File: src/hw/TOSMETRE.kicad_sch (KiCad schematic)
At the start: 61 parts, among them J1 Barrel_Jack_Switch, J2 Conn_01x02_Male, J3 Conn_01x08_Male, J4 Conn_Coaxial, J5 Conn_01x05_Male, J6 Conn_01x02_Male, J7 Conn_Coaxial, SW1 SW_DIP_x01, U1 TPS70950DBVT, U2 18F1320, U3 LT1818, U4 LTC2305, U5 LT1818

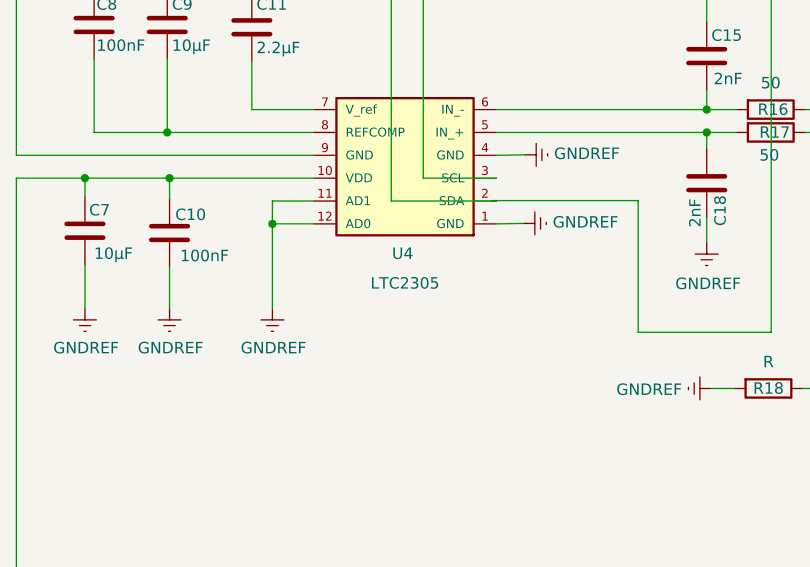
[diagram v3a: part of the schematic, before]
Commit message: #406
erreur danns la net liste
le U4 etait un 8plot alors qu'il en faut 12
rectif faite
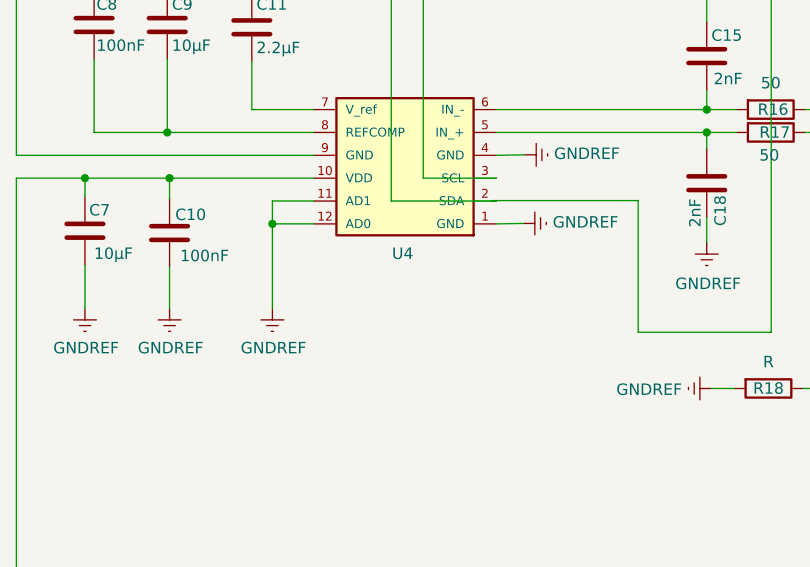
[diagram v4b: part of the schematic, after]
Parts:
- U4: value LTC2305 -> (none); footprint Package_SO:MSOP-8_3x3mm_P0.65mm -> (none)
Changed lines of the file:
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@@
     (in_bom yes) (on_board yes)
     (property "Reference" "U4" (id 0) (at 242.062 122.682 0))
-    (property "Value" "LTC2305" (id 1) (at 242.316 125.984 0))
-    (property "Footprint" "Package_SO:MSOP-8_3x3mm_P0.65mm" (id 2) (at 266.446 104.14 0)
+    (property "Value" "" (id 1) (at 242.316 125.984 0))
+    (property "Footprint" "" (id 2) (at 266.446 104.14 0)
       (effects (font (size 1.27 1.27)) hide)
     )
@@
     )
     (path "/00000000-0000-0000-0000-0000604b2f63"
-      (reference "U4") (unit 1) (value "LTC2305") (footprint "Package_SO:MSOP-8_3x3mm_P0.65mm")
+      (reference "U4") (unit 1) (value "LTC2305") (footprint "Package_SO:MSOP-12_3x4mm_P0.65mm")
     )
     (path "/00000000-0000-0000-0000-000060639a0d"

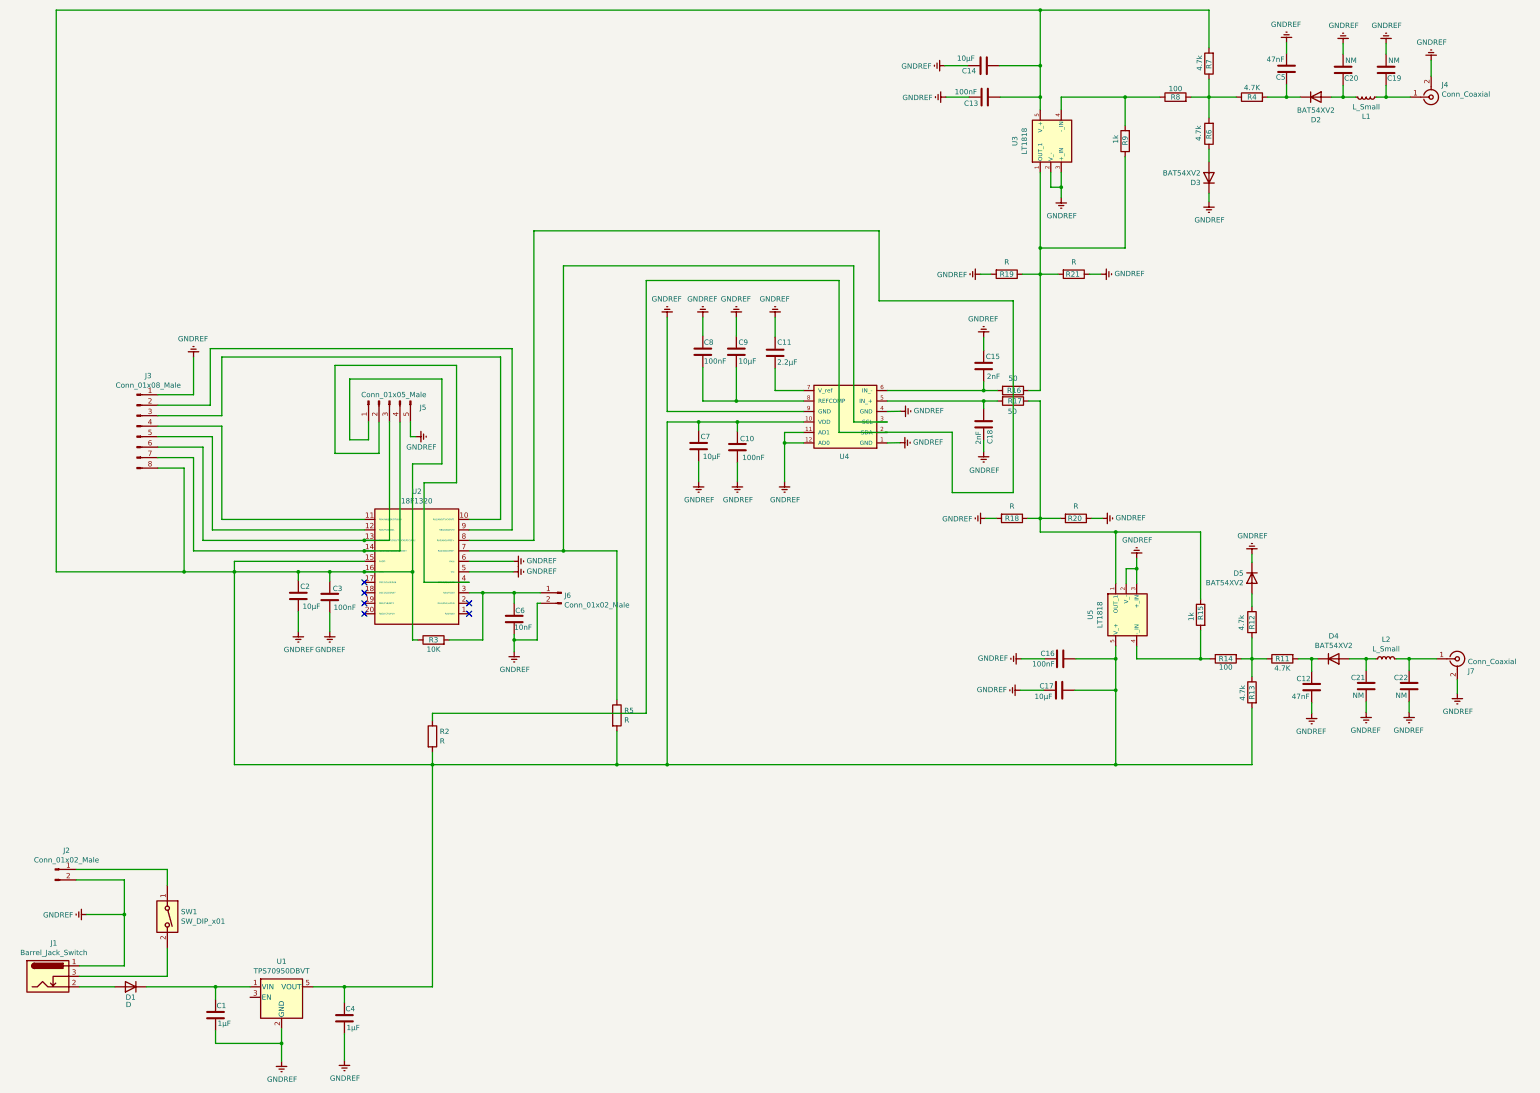
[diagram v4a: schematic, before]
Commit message: #406
PB termine
Nouvelle appleation suite a mauvaise manip (GRRRR) desole

Voir si on peux pas changer R1et R2 pour eviter qu'une piste passe dessous
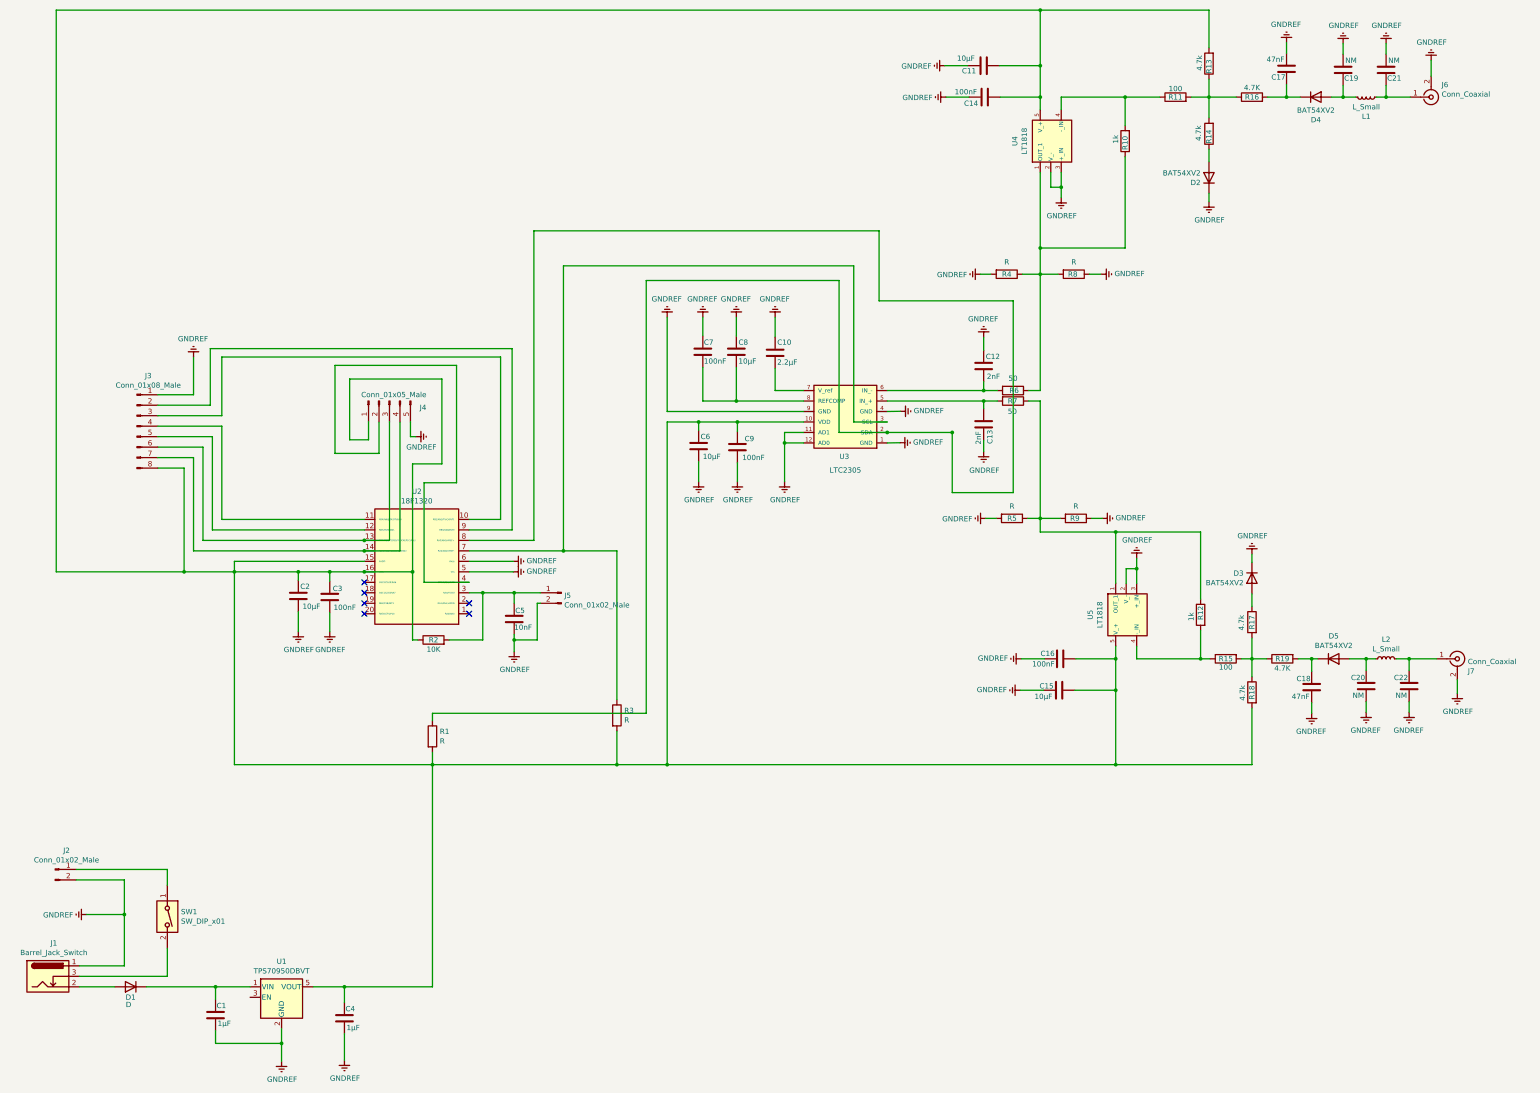
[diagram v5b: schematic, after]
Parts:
- U3: renamed from U4; value (none) -> LTC2305; footprint (none) -> Package_SO:MSOP-12_3x4mm_P0.65mm
- renumbered C11 to C10, C14 to C11, C15 to C12, C18 to C13, C13 to C14, C17 to C15, C5 to C17, C12 to C18, C20 to C19, C21 to C20, C19 to C21, C6 to C5, C7 to C6, C8 to C7, C9 to C8, C10 to C9, D3 to D2, D5 to D3, D2 to D4, D4 to D5, J5 to J4, J6 to J5, J4 to J6, R2 to R1, R9 to R10, R8 to R11, R15 to R12, R7 to R13, R6 to R14, R14 to R15, R4 to R16, R12 to R17, R13 to R18, R11 to R19, R3 to R2, R5 to R3, R19 to R4, R18 to R5, R16 to R6, R17 to R7, R21 to R8, R20 to R9, U3 to U4
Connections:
- net at U2.8 (RA3/AN3/VREF+): now also R1.1, U3.2 (SDA)

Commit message: #406
test
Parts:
- U4: renamed from U3; value LTC2305 -> (none); footprint Package_SO:MSOP-12_3x4mm_P0.65mm -> (none)
- renumbered C9 to C10, C10 to C11, C18 to C12, C14 to C13, C11 to C14, C12 to C15, C15 to C17, C13 to C18, C21 to C19, C19 to C20, C20 to C21, C17 to C5, C5 to C6, C6 to C7, C7 to C8, C8 to C9, D4 to D2, D2 to D3, D5 to D4, D3 to D5, J6 to J4, J4 to J5, J5 to J6, R19 to R11, R17 to R12, R18 to R13, R15 to R14, R12 to R15, R6 to R16, R7 to R17, R5 to R18, R4 to R19, R1 to R2, R9 to R20, R8 to R21, R2 to R3, R16 to R4, R3 to R5, R14 to R6, R13 to R7, R11 to R8, R10 to R9, U4 to U3
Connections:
- net at R2.1, U4.2 (SDA): no longer U2.8 (RA3/AN3/VREF+)

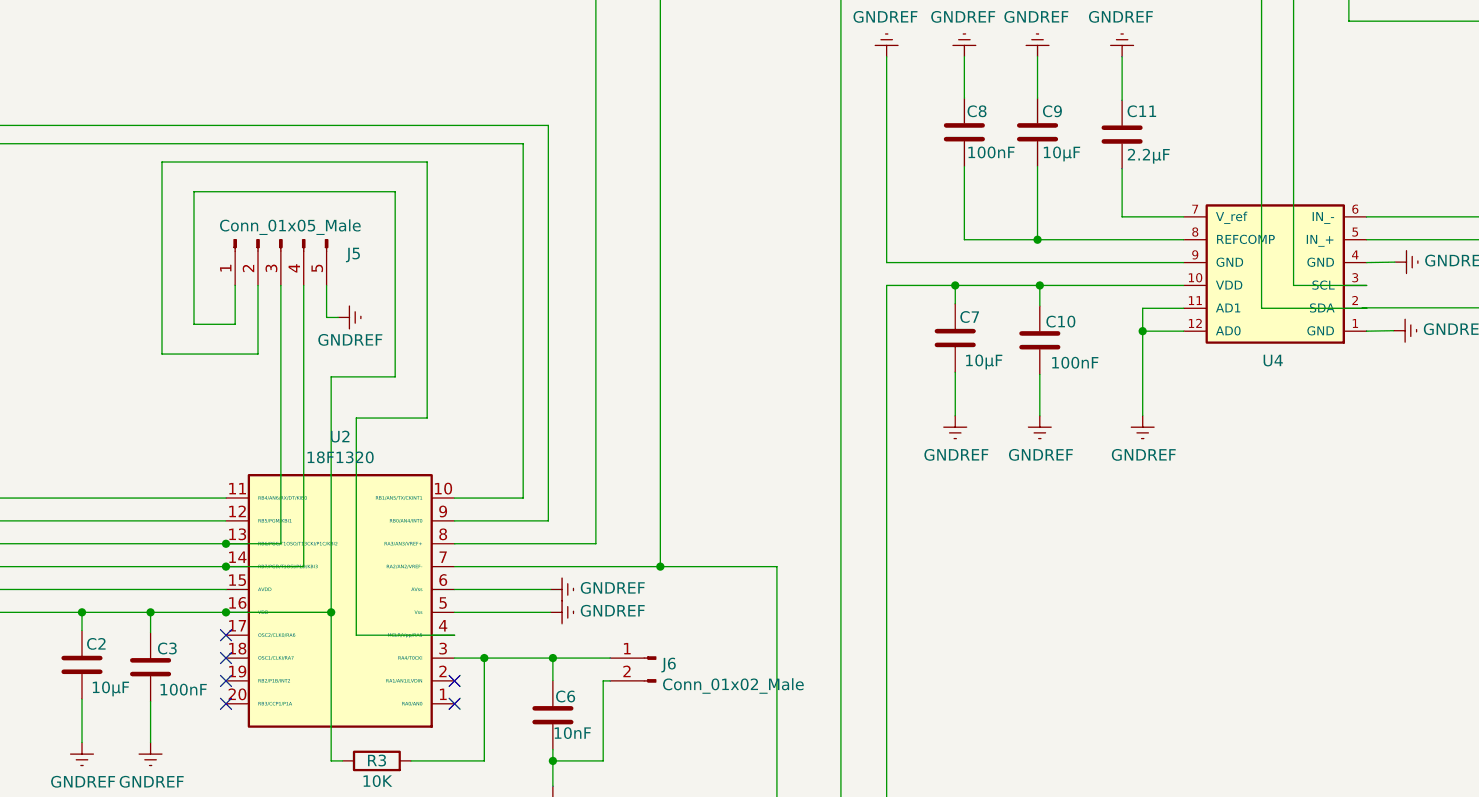
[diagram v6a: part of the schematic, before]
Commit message: #410
Modif Schema et routage sur J5 a valider par grand MANITOU
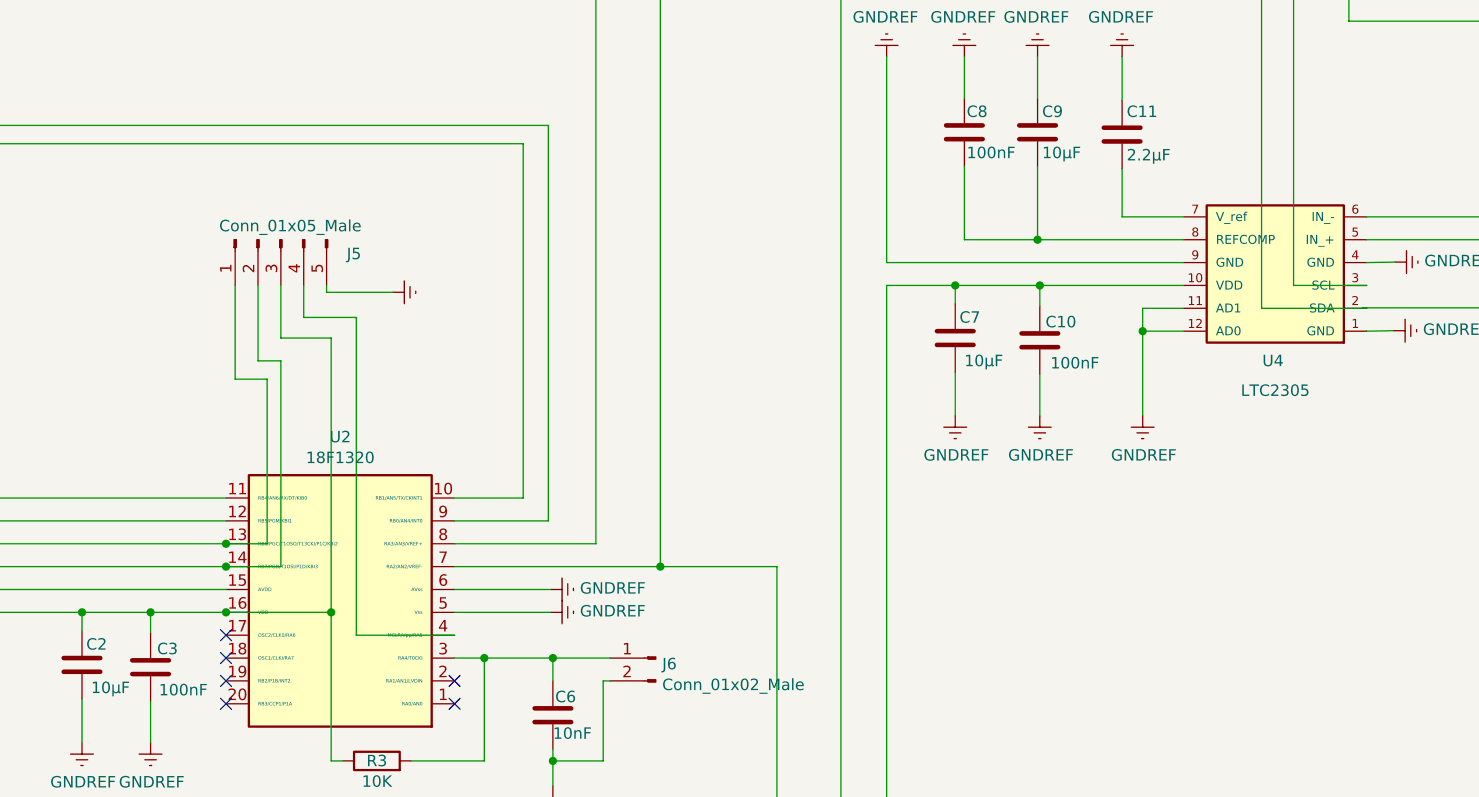
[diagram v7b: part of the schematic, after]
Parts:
- U4: value (none) -> LTC2305; footprint (none) -> Package_SO:MSOP-12_3x4mm_P0.65mm
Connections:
- net at J3.6 (Pin_6), U2.13 (RB6/PGC/T1OSO/T13CKI/P1C/KBI2): now also J5.1 (Pin_1); no longer J5.3 (Pin_3)
- net at J3.7 (Pin_7), U2.14 (RB7/PGD/T1OSI/P1D/KBI3): now also J5.2 (Pin_2); no longer J5.4 (Pin_4)
- net at C10.2, C13.2, C14.2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: now also J5.3 (Pin_3); no longer J5.1 (Pin_1)
- net at U2.4 (MCLR/Vpp/RA5): now also J5.4 (Pin_4); no longer J5.2 (Pin_2)

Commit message: #417
RACCORDEMENT BORNE 8 DE u2

Mauvaise connection dans le schema donc  la netliste ne le voyait pas

rectif faite
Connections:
- net at U2.8 (RA3/AN3/VREF+): now also R2.1, U4.2 (SDA)
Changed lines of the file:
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@@
   (junction (at 109.728 150.622) (diameter 0) (color 0 0 0 0)
+  )
+  (junction (at 252.476 116.84) (diameter 0) (color 0 0 0 0)
   )
   (junction (at 310.134 35.56) (diameter 0) (color 0 0 0 0)
@@
     (stroke (width 0) (type default) (color 0 0 0 0))
   )
-  (wire (pts (xy 251.968 116.7892) (xy 268.224 116.7892))
+  (wire (pts (xy 252.476 116.84) (xy 268.732 116.84))
     (stroke (width 0) (type default) (color 0 0 0 0))
   )
@@
     (stroke (width 0) (type default) (color 0 0 0 0))
   )
-  (wire (pts (xy 268.224 116.7892) (xy 268.224 131.4196))
+  (wire (pts (xy 268.732 116.84) (xy 268.224 131.4196))
     (stroke (width 0) (type default) (color 0 0 0 0))
   )
@@
       (effects (font (size 1.27 1.27)) hide)
     )
-    (property "Value" "" (id 1) (at 148.59 115.0619 90)
+    (property "Value" "GNDREF" (id 1) (at 148.59 115.0619 90)
       (effects (font (size 1.27 1.27)) (justify right))
     )
